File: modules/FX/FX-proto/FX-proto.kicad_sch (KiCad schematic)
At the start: 25 parts

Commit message: FX module - PCB prototype wip
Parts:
- added C1, C2: 10U, -lmp-misc:CP_Radial_D5.0mm_P2.50mm, symbol -lmp-synth:CP_10U
- added C3, C4, C6: 100N, -lmp-misc:C_Disc_D5.0mm_W2.5mm_P2.50mm, symbol -lmp:CC_100N
- added J1, J2: WQP-PJ398, -lmp-synth:Jack_3.5mm_QingPu_WQP-PJ398SM_Vertical, symbol -lmp-synth:Jack_WQP-PJ398
- added J3: Conn_Eurorack_16, -lmp-synth:IDC-Header-Eurorack-10-TH, symbol -lmp-synth:Conn_Eurorack_Pwr_10
- R2: renamed from R?; footprint -lmp-stripboard:SB_Gen_6 -> -lmp-misc:R_Axial_DIN0207_L6.3mm_D2.5mm_P7.62mm_Horizontal
- R3, R6: renamed from R?; footprint -lmp-stripboard:SB_Gen_1 -> -lmp-misc:R_Axial_DIN0207_L6.3mm_D2.5mm_P7.62mm_Horizontal
- R4: renamed from R?; footprint -lmp-stripboard:SB_Gen_4 -> -lmp-misc:R_Axial_DIN0207_L6.3mm_D2.5mm_P7.62mm_Horizontal
- R7: renamed from R?; footprint -lmp-stripboard:SB_Gen_2 -> -lmp-misc:R_Axial_DIN0207_L6.3mm_D2.5mm_P7.62mm_Horizontal
- RV1, RV2: renamed from RV?; footprint -lmp-misc:Potentiometer_Bourns_3310R_Top -> -lmp-synth:Potentiometer_SongHuei_Single_Vertical; symbol -lmp:R_POT_TRIM -> -lmp-synth:R_POT_TRIM_Panel_SongHuei; Distributor (none) -> SynthCube; Distributor2 (none) -> Thonk; DistributorPartLink (none) -> https://synthcube.com/cart/9mm-trimmer-pots; DistributorPartLink2 (none) -> https://www.thonk.co.uk/shop/ttpots/; DistributorPartNum (none) -> SH9MMTPOTMSTR; DistributorPartNum2 (none) -> Group_SongHuei_TTP; Manufacturer (none) -> Song Huei; ManufacturerPartNum (none) -> R0904N*
- RV3, RV4: renamed from RV?; footprint -lmp-misc:Potentiometer_Bourns_3386P_Top -> -lmp-synth:Potentiometer_SongHuei_Single_Vertical; symbol -lmp:R_POT_TRIM -> -lmp-synth:R_POT_TRIM_Panel_SongHuei; Distributor (none) -> SynthCube; Distributor2 (none) -> Thonk; DistributorPartLink (none) -> https://synthcube.com/cart/9mm-trimmer-pots; DistributorPartLink2 (none) -> https://www.thonk.co.uk/shop/ttpots/; DistributorPartNum (none) -> SH9MMTPOTMSTR; DistributorPartNum2 (none) -> Group_SongHuei_TTP; Manufacturer (none) -> Song Huei; ManufacturerPartNum (none) -> R0904N*
- gave numbers to parts that had none: 12
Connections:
- net +12V: now also C1.1, C3.1, J3.10, J3.9 (+12V)
- net +8V: now also C6.1
- net -12V: now also C2.2, C4.2, J3.1 (-12V), J3.2
- net GND: now also C1.2, C2.1, C3.2, C4.1, C6.2, J1.S, J1.TN, J2.S, J3.3 (GND), J3.4, J3.5 (GND), J3.6, J3.7 (GND), J3.8
- net ABE-CTL1: no longer names the net of A1.6 (CTL1), RV4.2
- net ABE-CTL2: no longer names the net of A1.5 (CTL2), RV3.2
- net ABE-CTL3: no longer names the net of A1.4 (CTL3), RV2.2
- net ABE-CTL4: no longer names the net of A1.3 (CTL4), RV1.2
- net ABE-CTL5: no longer names the net of A1.2 (CTL5), R1.1
- net ABE-VPOT: no longer names the net of A1.1 (VPOT), RV1.3, RV2.3, RV3.3, RV4.3
- net AUDIO-IN: no longer names the net of R2.1
- net AUDIO-IN: now also J1.T
- net AUDIO-OUT: no longer names the net of R10.2, U1.8
- net AUDIO-OUT: now also J2.T
- no-connect marks 7 -> 8
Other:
- removed sheet PanelPower
- note added: "100K should work for these"
- note removed: "Front Panel & Power"
- moved on the sheet: U1B, U1E, U2

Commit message: FX module - PCB prototype wip
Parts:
- SW1: footprint -lmp-breakout:Breakout_SW_Push_LED_C&K_D6R -> -lmp-synth:SW_Push_LED_C&K_D6R
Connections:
- net GND: now also U1.10 (+), U1.12 (+), U1.5 (+); no longer U1.10 (+), U1.3 (+)
- net at R2.2, R3.1: now also U1.6 (-); no longer U1.2 (-)
- net at C5.1, R3.2: now also U1.7; no longer U1.1
- net at R10.1, R8.2, R9.1: now also U1.13 (-); no longer U1.9 (-)
- net at C8.1, R5.2: now also U1.2 (-); no longer U1.13 (-)
- net at C7.1, R4.2: now also U1.3 (+); no longer U1.12 (+)
- net at C8.2, R7.2, R8.1: now also U1.1; no longer U1.14
- net at J2.T, R10.2: now also U1.14; no longer U1.8
- new net: U1.8, U1.9 (-)
- no-connect marks 8 -> 5
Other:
- note added: "TODO: connector for A1 in BOM"
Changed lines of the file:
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@@
   (junction (at 134.62 44.45) (diameter 0) (color 0 0 0 0)
   )
-  (no_connect (at 36.83 156.21))
   (no_connect (at 38.1 67.31))
-  (no_connect (at 36.83 161.29))
   (no_connect (at 208.28 46.99))
   (no_connect (at 38.1 77.47))
-  (no_connect (at 52.07 158.75))
   (no_connect (at 129.54 55.88))
   (no_connect (at 129.54 53.34))
@@
     (stroke (width 0) (type default) (color 0 0 0 0))
   )
+  (wire (pts (xy 33.02 156.21) (xy 33.02 157.48))
+    (stroke (width 0) (type default) (color 0 0 0 0))
+  )
   (wire (pts (xy 77.47 40.64) (xy 78.74 40.64))
     (stroke (width 0) (type default) (color 0 0 0 0))
@@
     (stroke (width 0) (type default) (color 0 0 0 0))
   )
+  (wire (pts (xy 52.07 158.75) (xy 53.34 158.75))
+    (stroke (width 0) (type default) (color 0 0 0 0))
+  )
+  (wire (pts (xy 53.34 158.75) (xy 53.34 168.91))
+    (stroke (width 0) (type default) (color 0 0 0 0))
+  )
   (wire (pts (xy 179.07 46.99) (xy 181.61 46.99))
     (stroke (width 0) (type default) (color 0 0 0 0))
@@
     (stroke (width 0) (type default) (color 0 0 0 0))
   )
+  (wire (pts (xy 36.83 156.21) (xy 33.02 156.21))
+    (stroke (width 0) (type default) (color 0 0 0 0))
+  )
   (wire (pts (xy 38.1 55.88) (xy 38.1 57.15))
     (stroke (width 0) (type default) (color 0 0 0 0))
@@
     (stroke (width 0) (type default) (color 0 0 0 0))
   )
+  (wire (pts (xy 53.34 168.91) (xy 35.56 168.91))
+    (stroke (width 0) (type default) (color 0 0 0 0))
+  )
   (wire (pts (xy 134.62 25.4) (xy 134.62 44.45))
     (stroke (width 0) (type default) (color 0 0 0 0))
@@
     (stroke (width 0) (type default) (color 0 0 0 0))
   )
+  (wire (pts (xy 35.56 168.91) (xy 35.56 161.29))
+    (stroke (width 0) (type default) (color 0 0 0 0))
+  )
   (wire (pts (xy 71.12 114.3) (xy 81.28 114.3))
     (stroke (width 0) (type default) (color 0 0 0 0))
@@
   )
   (wire (pts (xy 144.78 49.53) (xy 143.51 49.53))
+    (stroke (width 0) (type default) (color 0 0 0 0))
+  )
+  (wire (pts (xy 35.56 161.29) (xy 36.83 161.29))
     (stroke (width 0) (type default) (color 0 0 0 0))
   )
@@
     (effects (font (size 1.27 1.27)) (justify left bottom))
   )
+  (text "TODO: connector for A1 in BOM" (at 102.87 71.12 0)
+    (effects (font (size 1.27 1.27)) (justify left bottom))
+  )
   (text "100K should work for these" (at 50.8 88.9 0)
     (effects (font (size 1.27 1.27)) (justify left bottom))
@@
     (pin "2")
   )
-  (symbol (lib_id "-lmp-opamp:TL074") (at 69.85 40.64 0) (mirror x) (unit 1)
+  (symbol (lib_id "-lmp-opamp:TL074") (at 69.85 40.64 0) (mirror x) (unit 2)
     (in_bom yes) (on_board yes) (fields_autoplaced)
     (property "Reference" "U1" (id 0) (at 69.85 47.7504 0))
@@
       (effects (font (size 1.27 1.27)) (justify right))
     )
-    (property "Footprint" "-lmp-breakout:Breakout_SW_Push_LED_C&K_D6R" (id 2) (at 45.72 72.39 0)
+    (property "Footprint" "-lmp-synth:SW_Push_LED_C&K_D6R" (id 2) (at 45.72 72.39 0)
       (effects (font (size 1.27 1.27)) hide)
     )
@@
     (pin "1")
   )
-  (symbol (lib_id "-lmp-opamp:TL074") (at 44.45 158.75 0) (unit 2)
+  (symbol (lib_id "-lmp-opamp:TL074") (at 44.45 158.75 0) (unit 3)
     (in_bom yes) (on_board yes) (fields_autoplaced)
     (property "Reference" "U1" (id 0) (at 44.45 149.9702 0))
@@
     (pin "4")
   )
-  (symbol (lib_id "-lmp-opamp:TL074") (at 153.67 46.99 0) (unit 4)
+  (symbol (lib_id "-lmp-opamp:TL074") (at 153.67 46.99 0) (unit 1)
     (in_bom yes) (on_board yes)
     (property "Reference" "U1" (id 0) (at 157.48 40.64 0))
@@
     (pin "3")
   )
-  (symbol (lib_id "-lmp-opamp:TL074") (at 194.31 49.53 0) (mirror x) (unit 3)
+  (symbol (lib_id "-lmp-opamp:TL074") (at 194.31 49.53 0) (mirror x) (unit 4)
     (in_bom yes) (on_board yes) (fields_autoplaced)
     (property "Reference" "U1" (id 0) (at 194.31 56.6404 0))
@@
     (pin "1")
   )
+  (symbol (lib_id "-lmp-power:GND") (at 33.02 157.48 0) (unit 1)
+    (in_bom yes) (on_board yes) (fields_autoplaced)
+    (property "Reference" "#PWR0101" (id 0) (at 33.02 163.83 0)
+      (effects (font (size 1.27 1.27)) hide)
+    )
+    (property "Value" "GND" (id 1) (at 33.02 161.29 0)
+      (effects (font (size 1.27 1.27)) hide)
+    )
+    (property "Footprint" "" (id 2) (at 33.02 157.48 0)
+      (effects (font (size 1.27 1.27)) hide)
+    )
+    (property "Datasheet" "" (id 3) (at 33.02 157.48 0)
+      (effects (font (size 1.27 1.27)) hide)
+    )
+    (pin "1")
+  )
   (symbol (lib_id "-lmp-power:GND") (at 53.34 123.19 0) (unit 1)
     (in_bom yes) (on_board yes)
@@
       (reference "#PWR012") (unit 1) (value "GND") (footprint "")
     )
+    (path "/efc0b541-c2b5-4670-b7da-c34ee46b0243"
+      (reference "#PWR0101") (unit 1) (value "GND") (footprint "")
+    )
     (path "/d5f13f88-5ce5-41fc-8723-1d0e6c1cbb6d"
       (reference "A1") (unit 1) (value "Module_ABE") (footprint "-lmp-synth:Module_ABE_Vert")
@@
     )
     (path "/15358bc9-b991-48c5-b15f-fb3b0c574570"
-      (reference "SW1") (unit 1) (value "SW_LED") (footprint "-lmp-breakout:Breakout_SW_Push_LED_C&K_D6R")
+      (reference "SW1") (unit 1) (value "SW_LED") (footprint "-lmp-synth:SW_Push_LED_C&K_D6R")
+    )
+    (path "/3d59f77d-2786-4d96-8018-2e9bd7af788c"
+      (reference "U1") (unit 1) (value "TL074") (footprint "Package_DIP:DIP-14_W7.62mm")
     )
     (path "/0fd8b9f7-dfef-4176-8be0-1ebfc2952e0b"
-      (reference "U1") (unit 1) (value "TL074") (footprint "Package_DIP:DIP-14_W7.62mm")
+      (reference "U1") (unit 2) (value "TL074") (footprint "Package_DIP:DIP-14_W7.62mm")
     )
     (path "/3c545c12-15bf-4dbb-90de-af5385a9dd5c"
-      (reference "U1") (unit 2) (value "TL074") (footprint "Package_DIP:DIP-14_W7.62mm")
+      (reference "U1") (unit 3) (value "TL074") (footprint "Package_DIP:DIP-14_W7.62mm")
     )
     (path "/dd1d7209-b5cc-486d-8e2e-25909818ed19"
-      (reference "U1") (unit 3) (value "TL074") (footprint "Package_DIP:DIP-14_W7.62mm")
-    )
-    (path "/3d59f77d-2786-4d96-8018-2e9bd7af788c"
       (reference "U1") (unit 4) (value "TL074") (footprint "Package_DIP:DIP-14_W7.62mm")
     )

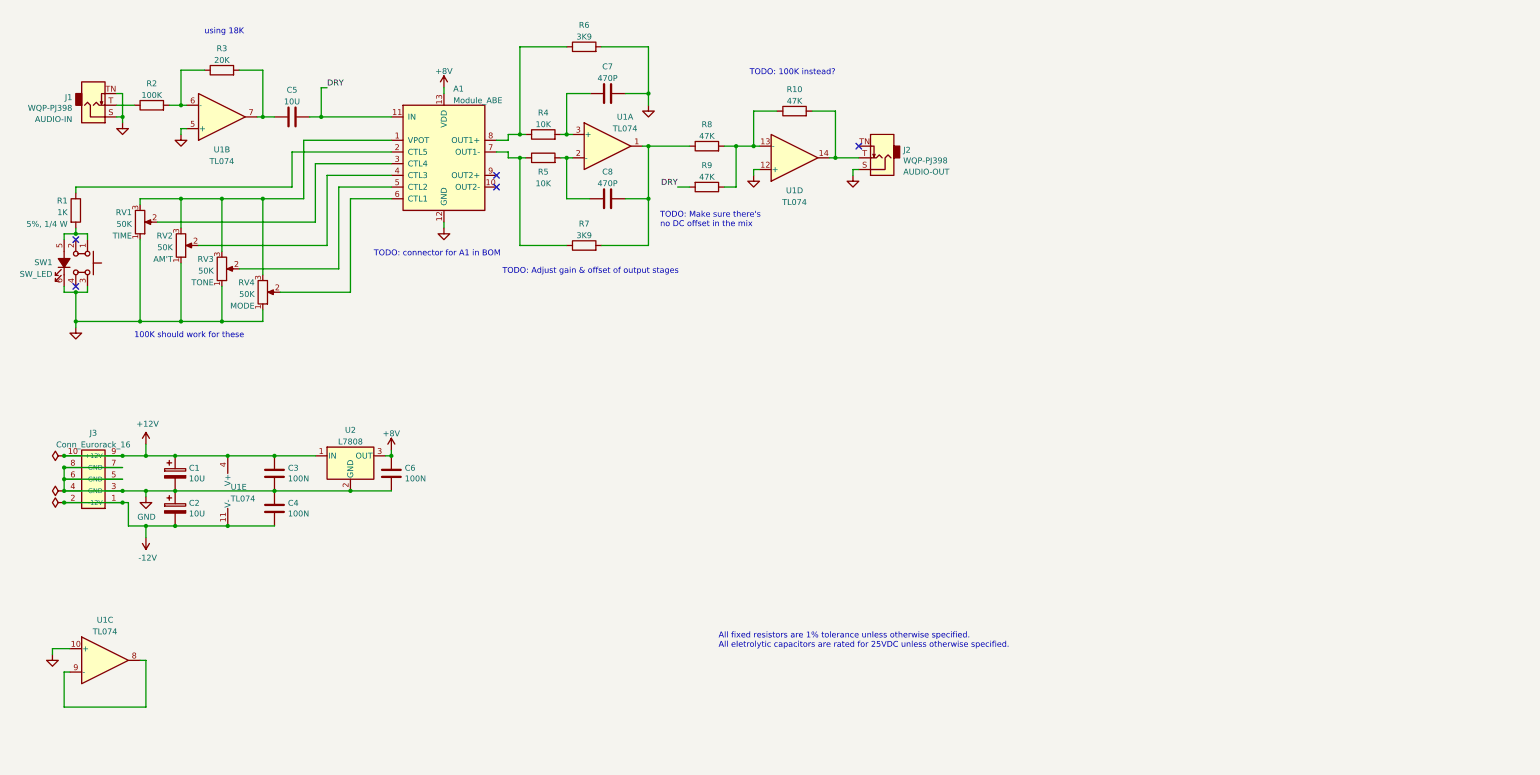
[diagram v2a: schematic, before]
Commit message: FX module - PCB prototype - layout done
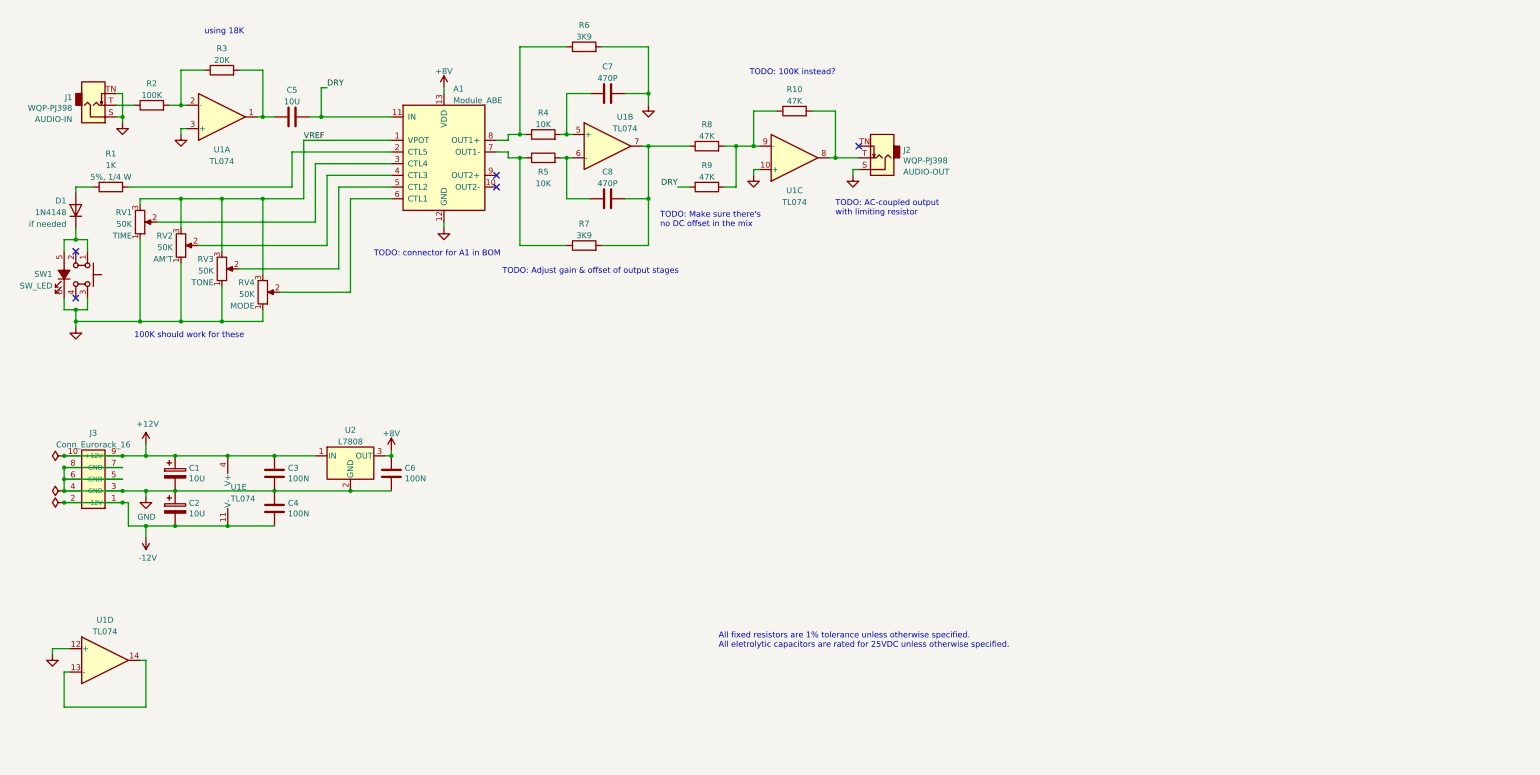
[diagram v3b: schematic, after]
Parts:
- added D1: 1N4148, Diode_THT:D_DO-35_SOD27_P7.62mm_Horizontal, symbol -lmp-diode:1N4148
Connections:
- net GND: now also U1.10 (+), U1.12 (+), U1.3 (+); no longer U1.10 (+), U1.12 (+), U1.5 (+)
- net at R2.2, R3.1: now also U1.2 (-); no longer U1.6 (-)
- net at C5.1, R3.2: now also U1.1; no longer U1.7
- net at R10.1, R8.2, R9.1: now also U1.9 (-); no longer U1.13 (-)
- net at SW1.1, SW1.5 (A): now also D1.1 (K); no longer R1.2
- net at C8.1, R5.2: now also U1.6 (-); no longer U1.2 (-)
- net at C8.2, R7.2, R8.1: now also U1.7; no longer U1.1
- net at C7.1, R4.2: now also U1.5 (+); no longer U1.3 (+)
- net at J2.T, R10.2: now also U1.8; no longer U1.14
- net VREF: now reaches A1.1 (VPOT), RV1.3, RV2.3, RV3.3, RV4.3
- new net: U1.13 (-), U1.14
- new net: D1.2 (A), R1.2
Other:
- note added: "TODO: AC-coupled output with limiting resistor"
- moved on the sheet: R1, SW1

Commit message: FX module - PCB prototype - mix control
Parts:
- removed R8, R9: 47K, -lmp-misc:R_Axial_DIN0207_L6.3mm_D2.5mm_P7.62mm_Horizontal, symbol -lmp:R_1%_0W166
- added C9: 10U, -lmp-misc:C_Radial_D5.0mm_H5.0mm_P2.50mm, symbol -lmp-synth:CNP_10U
- added R11: 100K, -lmp-misc:R_Axial_DIN0207_L6.3mm_D2.5mm_P7.62mm_Horizontal, symbol -lmp:R_1%_0W166
- added R12: 1K, -lmp-misc:R_Axial_DIN0207_L6.3mm_D2.5mm_P10.16mm_Horizontal, symbol -lmp-synth:R_1K_Output
- added RV5: 50K, -lmp-synth:Potentiometer_SongHuei_Single_Vertical, symbol -lmp-synth:R_POT_TRIM_Panel_SongHuei
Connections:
- net DRY: now also RV5.1
- net GND: now also R11.2
- net at R10.1, U1.9 (-): now also RV5.2
- net at C8.2, R7.2, U1.7: now also RV5.3
- net at R10.2, U1.8: now also C9.1; no longer J2.T
- new net: C9.2, R11.1, R12.1
- new net: J2.T, R12.2
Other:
- note added: "TODO: connector for A1 in BOM?"
- note removed: "TODO: AC-coupled output with limiting resistor"
- note removed: "TODO: connector for A1 in BOM"
- moved on the sheet: A1, C1, C2, C3, C4, C5, C6, C7, C8, D1, J1, J2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

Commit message: FX module - PCB prototype - wip
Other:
- note added: "TODO: How to balance wet & dry levels"
- note added: "TODO: Other output channel"
- moved on the sheet: A1, C7, C8, R4, R5, R6, R7, U1B

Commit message: FX module - prototype wip
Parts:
- R6, R7: value 3K9 -> 2K2
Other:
- note added: "Input stage reduces input signal to nominal 2Vp-p"
- note added: "PROBLEM: Voltage offset: dry is 0-2V, wet is -1-+1V"
- note added: "R6 & R7 set gain to produce 2Vp-p signal, matching the input."
- note removed: "TODO: Adjust gain & offset of output stages"
- note removed: "TODO: How to balance wet & dry levels"
- note removed: "TODO: Make sure there's no DC offset in the mix"
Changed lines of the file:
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@@
     (stroke (width 0) (type default) (color 0 0 0 0))
   )
-  (text "TODO: How to balance \nwet & dry levels" (at 157.48 78.74 0)
+  (text "Input stage reduces input \nsignal to nominal 2Vp-p"
+    (at 40.64 39.37 0)
     (effects (font (size 1.27 1.27)) (justify left bottom))
   )
@@
     (effects (font (size 1.27 1.27)) (justify left bottom))
   )
-  (text "TODO: Adjust gain & offset of output stages" (at 123.19 87.63 0)
+  (text "R6 & R7 set gain to produce \n2Vp-p signal, matching the input."
+    (at 125.73 88.9 0)
     (effects (font (size 1.27 1.27)) (justify left bottom))
   )
@@
     (effects (font (size 1.27 1.27)) (justify left bottom))
   )
-  (text "TODO: Make sure there's \nno DC offset in the mix" (at 157.48 72.39 0)
+  (text "PROBLEM: Voltage offset: \ndry is 0-2V, wet is -1-+1V"
+    (at 157.48 72.39 0)
     (effects (font (size 1.27 1.27)) (justify left bottom))
   )
@@
     (effects (font (size 1.27 1.27)) (justify left bottom))
   )
-  (text "using 18K" (at 66.04 35.56 0)
+  (text "using 18K" (at 64.77 46.99 0)
     (effects (font (size 1.27 1.27)) (justify left bottom))
   )
@@
     (in_bom yes) (on_board yes) (fields_autoplaced)
     (property "Reference" "R7" (id 0) (at 140.97 76.5642 90))
-    (property "Value" "3K9" (id 1) (at 140.97 79.1011 90))
+    (property "Value" "2K2" (id 1) (at 140.97 79.1011 90))
     (property "Footprint" "-lmp-misc:R_Axial_DIN0207_L6.3mm_D2.5mm_P7.62mm_Horizontal" (id 2) (at 140.97 83.058 90)
       (effects (font (size 1.27 1.27)) hide)
@@
     (in_bom yes) (on_board yes) (fields_autoplaced)
     (property "Reference" "R6" (id 0) (at 140.97 33.3842 90))
-    (property "Value" "3K9" (id 1) (at 140.97 35.9211 90))
+    (property "Value" "2K2" (id 1) (at 140.97 35.9211 90))
     (property "Footprint" "-lmp-misc:R_Axial_DIN0207_L6.3mm_D2.5mm_P7.62mm_Horizontal" (id 2) (at 140.97 39.878 90)
       (effects (font (size 1.27 1.27)) hide)
@@
     )
     (path "/47f2a6d4-21f5-4a5e-8df4-18181cdeae5d"
-      (reference "R6") (unit 1) (value "3K9") (footprint "-lmp-misc:R_Axial_DIN0207_L6.3mm_D2.5mm_P7.62mm_Horizontal")
+      (reference "R6") (unit 1) (value "2K2") (footprint "-lmp-misc:R_Axial_DIN0207_L6.3mm_D2.5mm_P7.62mm_Horizontal")
     )
     (path "/3f350e6d-335e-46fb-9030-33a06d5f0a21"
-      (reference "R7") (unit 1) (value "3K9") (footprint "-lmp-misc:R_Axial_DIN0207_L6.3mm_D2.5mm_P7.62mm_Horizontal")
+      (reference "R7") (unit 1) (value "2K2") (footprint "-lmp-misc:R_Axial_DIN0207_L6.3mm_D2.5mm_P7.62mm_Horizontal")
     )
     (path "/70b9914f-0138-470a-a07d-e1a88a53471e"
